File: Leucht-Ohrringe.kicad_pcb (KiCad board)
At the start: 2 copper layers, 20 x 49.5 mm, 39 parts, among them J1 Conn_ARM_SWD_TagConnect_TC2030, P1 USB_C_Plug_USB2.0, U4 CH340N, U5 nRF52832-QFxx

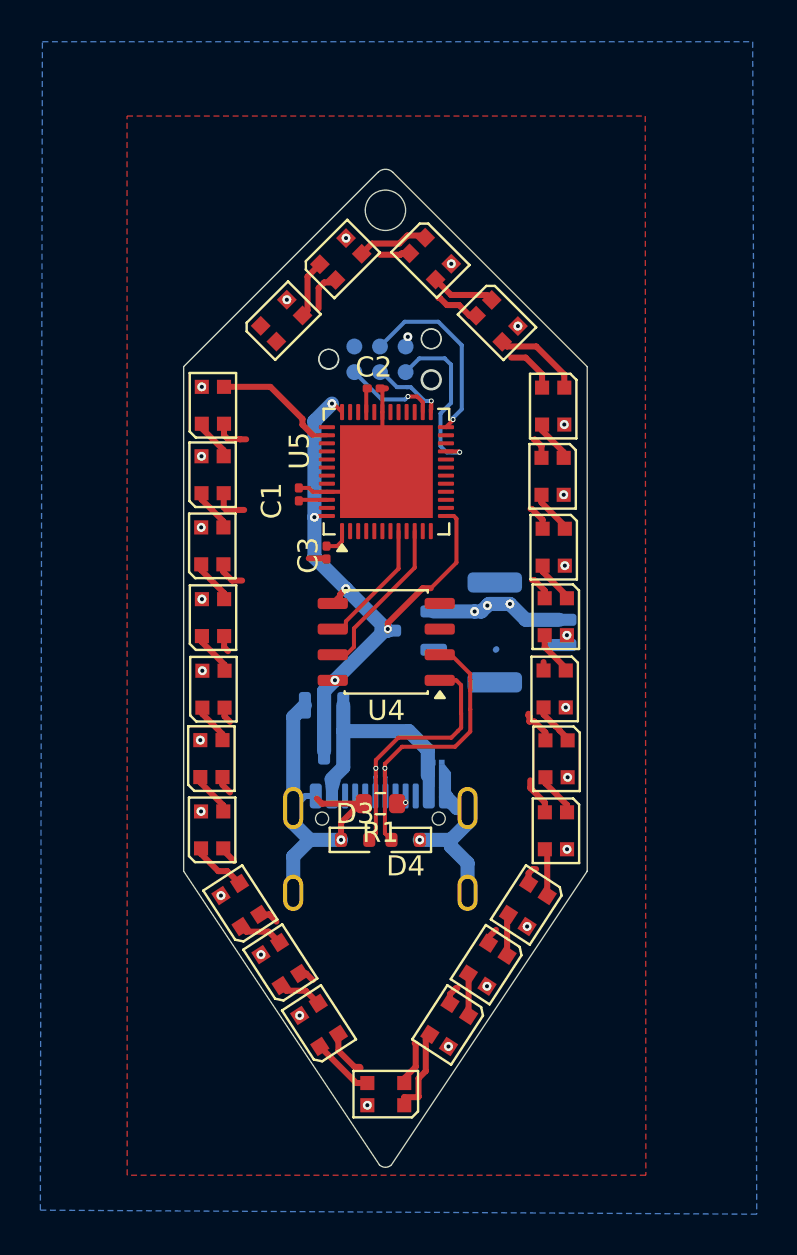
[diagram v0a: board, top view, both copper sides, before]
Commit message: add smd antenna, change usb to uart ic to smaller packag
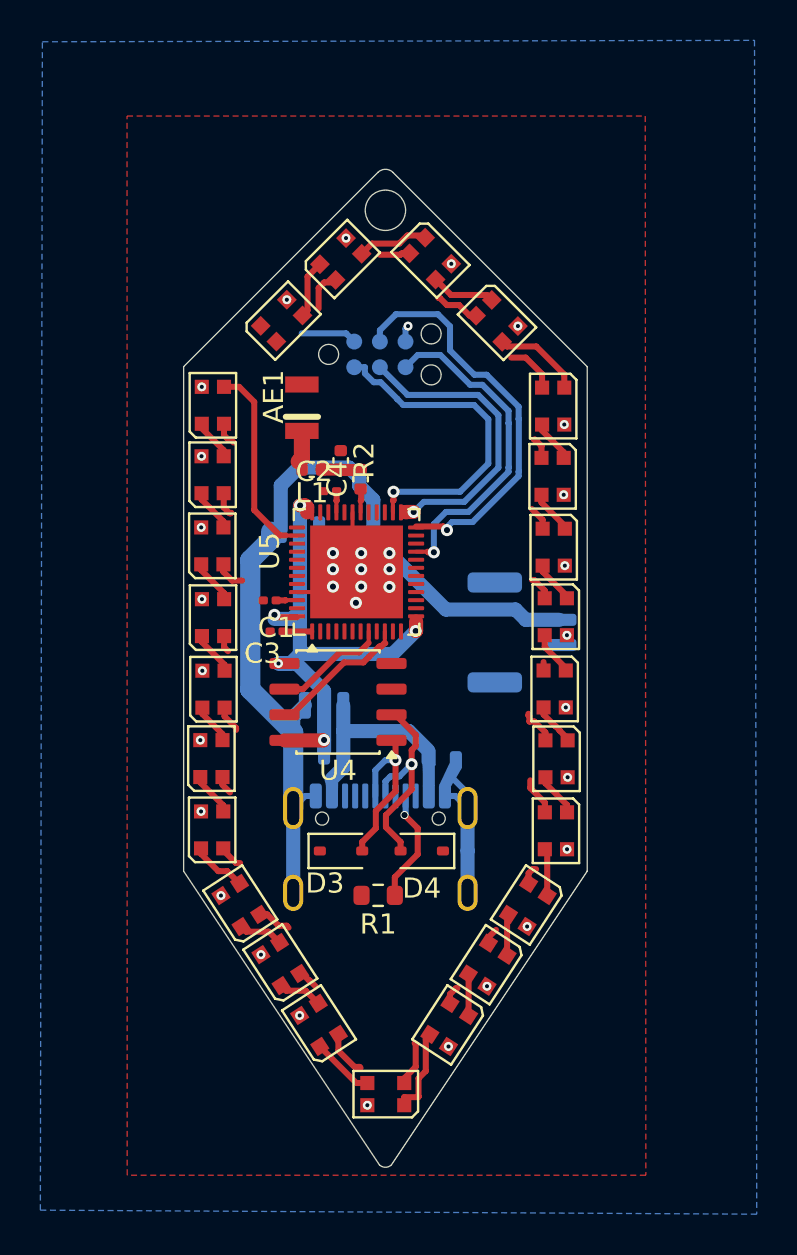
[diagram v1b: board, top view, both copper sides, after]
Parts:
- added AE1: Antenna_Chip, Package_TO_SOT_SMD:RFANT3216120A5T, F.Cu at (160.9, 63.2)
- added C4: 0, Capacitor_SMD:C_0402_1005Metric, F.Cu at (163.8, 65.6)
- added L1: 0, Capacitor_SMD:C_0402_1005Metric, F.Cu at (161.3, 65.1)
- added R2: 0, Capacitor_SMD:C_0402_1005Metric, F.Cu at (162.8, 64.6)
- D2: value ESD411 -> ESD5Z6.0; footprint Button_Switch_SMD:ESD411 -> Diode_SMD:D_SOD-523
- D3, D4: value ESD321 -> H4V5HD3UA; footprint Diode_SMD:D_SOD-523 -> Diode_SMD:D_SOD-323
- moved U1 6.72 mm to (160.8, 69.2), turned to -90 degrees
- moved C2 5.53 mm to (162.3, 66.2), turned to 180 degrees
- moved C1 5.45 mm to (159.3, 71.6), turned to 180 degrees
- moved U5 5.19 mm to (163.6, 70.2)
- moved C3 4.63 mm to (159.6, 73.1), turned to 180 degrees
- moved R1 4.55 mm to (164.6, 86.2)
- moved U4 3.82 mm to (162.7, 76.6)
- moved D4 0.97 mm to (166.8, 84.0)
- moved D3 0.89 mm to (162.8, 84.0)
- moved J1 0.24 mm to (164.7, 59.4)
- moved D2 0.20 mm to (167.8, 79.4)
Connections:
- U5 pad 30: unconnected-(U5-ANT-Pad30) -> Net-(U5-ANT)
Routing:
- net GND: track 76.6 -> 101.3 mm, vias 6 -> 11
- net Net-(J1-SWDIO): track 4.62 -> 16.4 mm
- net Net-(J1-SWCLK): track 3.69 -> 15.0 mm
- net Net-(J1-~{RESET}): track 9.43 -> 20.3 mm
- net Net-(J1-SWO): track 9.12 -> 16.6 mm
- net Net-(P1-CC): track 0.45 -> 5.69 mm
- net /D+: track 13.6 -> 9.02 mm
- net VDD: track 30.6 -> 26.5 mm
- net LED_IN: track 6.26 -> 9.81 mm
- net /D-: track 14.9 -> 11.6 mm
- net unconnected-(J1-VCC-Pad1): track 0.00 -> 2.77 mm
- net Net-(AE1-FEED): track 0.00 -> 2.05 mm
- net Net-(C4-Pad2): track 0.00 -> 1.96 mm
- net +5V: track 9.74 -> 8.48 mm
- net Net-(U5-ANT): track 0.00 -> 1.15 mm
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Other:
- outline, holes or cut-outs redrawn
- board text added: "B+"
- board text added: "B-"
- board text added: "VDD"

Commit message: replace battery voltage plane with trace
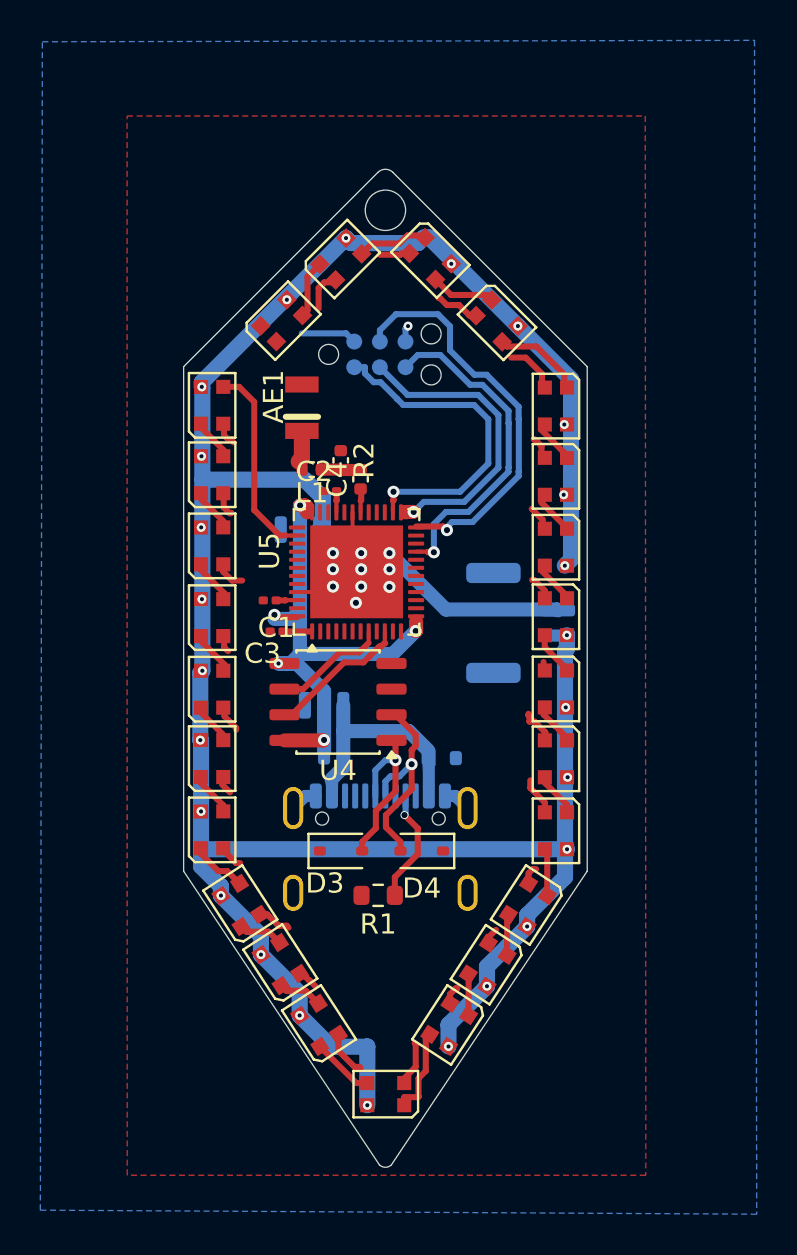
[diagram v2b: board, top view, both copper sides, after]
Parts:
- moved BT1 0.48 mm to (171.7, 72.7)
- moved D23 0.17 mm to (173.4, 65.4)
- moved D24 0.14 mm to (173.4, 62.0)
- moved D22 0.11 mm to (173.4, 68.9)
- moved D8 0.06 mm to (156.4, 76.0)
- moved D20 0.06 mm to (173.4, 76.0)
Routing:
- net +BATT: track 0.64 -> 123.1 mm
- net GND: track 101.3 -> 63.8 mm
- added copper zone on B.Cu, net GND
- removed copper zone on B.Cu, net +BATT

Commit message: add gerbers, fix reversed esd diodes
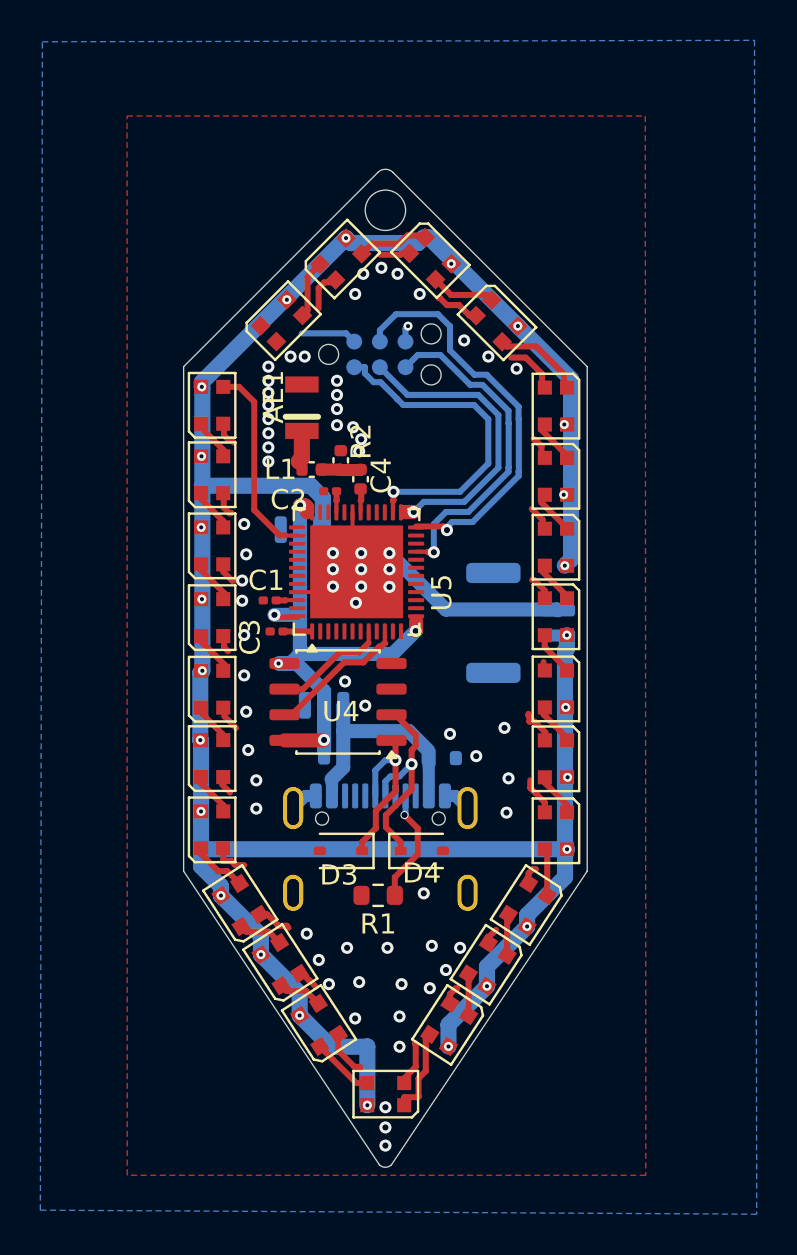
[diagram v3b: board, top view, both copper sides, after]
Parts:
- turned D2 to 0 degrees
- turned D3 to 180 degrees
- turned D4 to 0 degrees
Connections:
- D2 pad 1: GND -> +5V
- D2 pad 2: +5V -> GND
- D3 pad 1: GND -> /D+
- D3 pad 2: /D+ -> GND
- D4 pad 1: GND -> /D-
- D4 pad 2: /D- -> GND
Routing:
- net GND: track 63.8 -> 64.3 mm, vias 11 -> 71
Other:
- board text added: "GND"
- board text added: "RESET"
- board text added: "SWCLK"
- board text added: "SWDIO"
- board text added: "SWO"

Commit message: add 6-axis imu
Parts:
- added R3: 10k, Resistor_SMD:R_0402_1005Metric_Pad0.72x0.64mm_HandSolder, B.Cu at (169.3, 68.1)
- added R4: 10k, Resistor_SMD:R_0402_1005Metric_Pad0.72x0.64mm_HandSolder, B.Cu at (170.3, 68.1)
- added U3: ~, Package_LGA:Bosch_LGA-14_3x2.5mm_P0.5mm, F.Cu at (169.6, 70.8)
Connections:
- U5 pad 14: unconnected-(U5-P0.11-Pad14) -> Net-(U3-INT1)
- U5 pad 15: unconnected-(U5-P0.12-Pad15) -> Net-(U3-AP_AD0)
- U5 pad 16: unconnected-(U5-P0.13-Pad16) -> Net-(U3-AP_SDA)
- U5 pad 17: unconnected-(U5-P0.14-Pad17) -> Net-(U3-AP_SCL)
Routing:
- net GND: track 64.3 -> 45.5 mm
- net VDD: track 26.2 -> 40.5 mm, vias 5 -> 8
- net Net-(U3-AP_SDA): track 0.00 -> 9.79 mm, vias 0 -> 1
- net Net-(J1-SWDIO): track 16.4 -> 8.32 mm
- net Net-(J1-SWCLK): track 15.0 -> 8.27 mm
- net Net-(J1-SWO): track 16.6 -> 10.4 mm
- net Net-(U3-AP_SCL): track 0.00 -> 6.01 mm, vias 0 -> 1
- net Net-(U3-INT1): track 0.00 -> 4.73 mm
- net Net-(J1-~{RESET}): track 20.3 -> 17.3 mm
- net Net-(U3-AP_AD0): track 0.00 -> 2.53 mm
